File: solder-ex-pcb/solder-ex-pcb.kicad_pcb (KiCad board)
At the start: 2 copper layers, 38.1 x 25.4 mm, 3 parts

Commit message: added tester to solder exercise pcb
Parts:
- removed BT1: Batt, footprints:BATT
- added B1: Batt, footprints:BATT, F.Cu at (124.0, 63.5)
- added J1: Tester, footprints:BATT, B.Cu at (125.2, 54.9)
- moved R1 10.2 mm to (111.3, 68.6), turned to 90 degrees
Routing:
- net Net-(B1-Pad2): track 56.0 -> 42.8 mm
- net Net-(B1-Pad1): track 15.2 -> 26.6 mm
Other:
- board text added: "Tester"

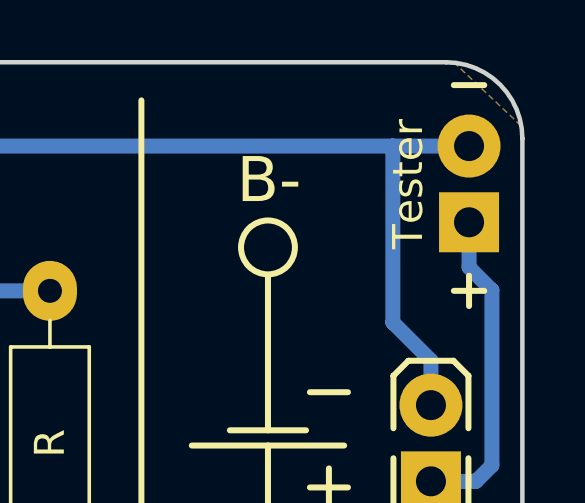
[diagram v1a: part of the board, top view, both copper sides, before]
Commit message: ordered version of the solder exercise pcb
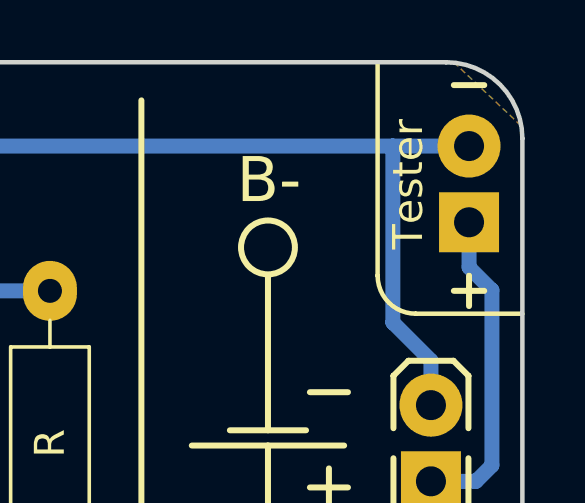
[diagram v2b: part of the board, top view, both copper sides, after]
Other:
- board text added: ":: solderex v1.0 :: mintpepper.ch ::"
- board text added: "R2.54mm"
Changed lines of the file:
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@@
-(kicad_pcb (version 20171130) (host pcbnew "(5.0.1)-3")
+(kicad_pcb (version 20171130) (host pcbnew "(5.1.4)-1")
   (general
     (thickness 1.6)
-    (drawings 115)
+    (drawings 124)
     (tracks 18)
     (zones 0)
@@
     (zone_45_only no)
     (trace_min 0.2)
-    (segment_width 0.2)
-    (edge_width 0.15)
     (via_size 0.8)
     (via_drill 0.4)
@@
     (uvia_min_size 0.2)
     (uvia_min_drill 0.1)
+    (edge_width 0.15)
+    (segment_width 0.2)
     (pcb_text_width 0.3)
     (pcb_text_size 1.5 1.5)
@@
     (pad_to_mask_clearance 0.051)
     (solder_mask_min_width 0.25)
-    (aux_axis_origin 0 0)
+    (aux_axis_origin 88.9 50.8)
+    (grid_origin 88.9 50.8)
     (visible_elements 7FFFFF7F)
     (pcbplotparams
-      (layerselection 0x010fc_ffffffff)
+      (layerselection 0x011f0_ffffffff)
       (usegerberextensions false)
       (usegerberattributes false)
@@
       (viasonmask false)
       (mode 1)
-      (useauxorigin false)
+      (useauxorigin true)
       (hpglpennumber 1)
       (hpglpenspeed 20)
@@
       (outputformat 1)
       (mirror false)
-      (drillshape 1)
+      (drillshape 0)
       (scaleselection 1)
-      (outputdirectory ""))
+      (outputdirectory "gerberV1.0"))
   )
   (net 0 "")
@@
     )
   )
+  (gr_text R2.54mm (at 135.636 78.486) (layer Dwgs.User)
+    (effects (font (size 1 1) (thickness 0.15)))
+  )
+  (gr_line (start 126.238 75.438) (end 133.096 78.232) (layer Dwgs.User) (width 0.15))
+  (gr_arc (start 123.444 57.912) (end 122.174 57.912) (angle -90) (layer F.SilkS) (width 0.15))
+  (gr_line (start 123.444 59.182) (end 127 59.182) (layer B.SilkS) (width 0.15))
+  (gr_line (start 122.174 50.8) (end 122.174 57.912) (layer F.SilkS) (width 0.15))
+  (gr_arc (start 123.444 57.912) (end 122.174 57.912) (angle -90) (layer B.SilkS) (width 0.15))
+  (gr_line (start 123.444 59.182) (end 127 59.182) (layer F.SilkS) (width 0.15))
+  (gr_line (start 122.174 50.8) (end 122.174 57.912) (layer B.SilkS) (width 0.15))
+  (gr_text ":: solderex v1.0 :: mintpepper.ch ::" (at 107.696 74.93) (layer B.SilkS)
+    (effects (font (size 1.2 1.2) (thickness 0.18)) (justify mirror))
+  )
   (gr_text Tester (at 123.19 54.864 90) (layer F.SilkS)
     (effects (font (size 1 1) (thickness 0.15)))
@@
     (arrow2b (pts (xy 86.36 50.8) (xy 86.946421 51.926504)))
   )
-  (gr_text DC (at 92.70573 54.903996 180) (layer B.SilkS)
+  (gr_text DC (at 92.70573 54.903996) (layer B.SilkS)
     (effects (font (size 1.5 1.5) (thickness 0.3)) (justify mirror))
   )
@@
   (gr_line (start 105.371658 60.244585) (end 105.371658 58.212585) (layer B.SilkS) (width 0.2))
   (gr_line (start 119.956406 64.99062) (end 121.226406 64.99062) (layer B.SilkS) (width 0.2))
-  (gr_line (start 114.3 74.93) (end 114.3 52.07) (layer B.SilkS) (width 0.2))
+  (gr_line (start 114.3 72.898) (end 114.3 52.07) (layer B.SilkS) (width 0.2))
   (gr_circle (center 92.70573 69.889996) (end 92.07073 69.254996) (layer B.SilkS) (width 0.2))
   (gr_line (start 120.591406 65.62562) (end 120.591406 64.35562) (layer B.SilkS) (width 0.2))
   (gr_circle (center 105.371658 69.896585) (end 104.736658 69.261585) (layer B.SilkS) (width 0.2))
   (gr_line (start 119.916296 61.798326) (end 121.186296 61.798326) (layer B.SilkS) (width 0.2))
-  (gr_line (start 101.6 74.93) (end 101.6 52.07) (layer B.SilkS) (width 0.2))
+  (gr_line (start 101.6 72.898) (end 101.6 52.07) (layer B.SilkS) (width 0.2))
   (gr_line (start 105.371658 66.594585) (end 105.371658 68.880585) (layer B.SilkS) (width 0.2))
   (gr_line (start 106.641658 66.594585) (end 106.641658 60.244585) (layer B.SilkS) (width 0.2))
